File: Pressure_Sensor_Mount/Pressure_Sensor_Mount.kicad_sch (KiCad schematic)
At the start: 2 parts, among them J1 Conn_01x04_Pin

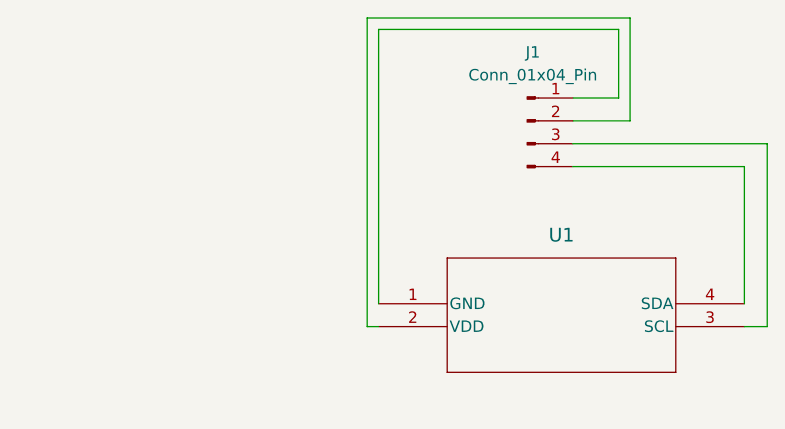
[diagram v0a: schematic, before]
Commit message: Modified boot.py and KiCad Schematic
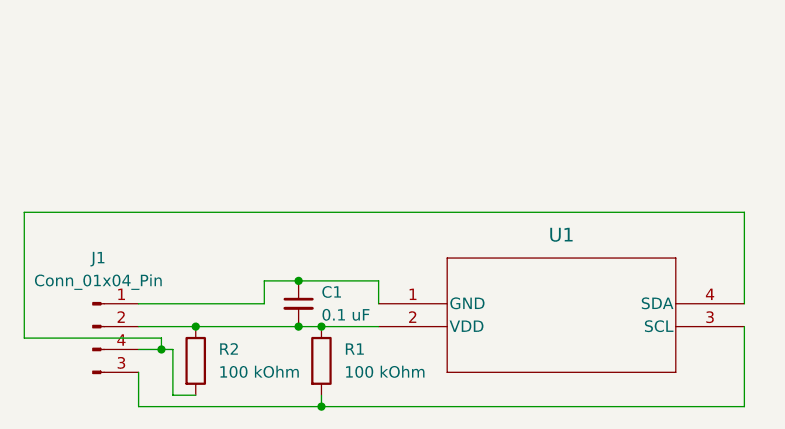
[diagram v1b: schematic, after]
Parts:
- added C1: 0.1 uF, symbol Device:C_Small
- added R1, R2: 100 kOhm, symbol Device:R
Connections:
- net at J1.1 (Pin_1), U1.1 (GND): now also C1.1
- net at J1.2 (Pin_2), U1.2 (VDD): now also C1.2, R1.1, R2.1
- net at J1.3 (Pin_3), U1.3 (SCL): now also R1.2
- net at J1.4 (Pin_4), U1.4 (SDA): now also R2.2
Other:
- moved on the sheet: J1
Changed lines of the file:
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@@
 (kicad_sch (version 20230121) (generator eeschema)
   (paper "A4")
-  (wire (pts (xy 140.97 92.71) (xy 160.02 92.71))
-    (stroke (width 0) (type default))
-  )
-  (wire (pts (xy 162.56 110.49) (xy 160.02 110.49))
-    (stroke (width 0) (type default))
-  )
-  (wire (pts (xy 147.32 76.2) (xy 147.32 87.63))
-    (stroke (width 0) (type default))
-  )
-  (wire (pts (xy 147.32 87.63) (xy 140.97 87.63))
-    (stroke (width 0) (type default))
-  )
-  (wire (pts (xy 160.02 107.95) (xy 160.02 92.71))
-    (stroke (width 0) (type default))
-  )
-  (wire (pts (xy 140.97 90.17) (xy 162.56 90.17))
-    (stroke (width 0) (type default))
-  )
-  (wire (pts (xy 162.56 90.17) (xy 162.56 110.49))
-    (stroke (width 0) (type default))
-  )
-  (wire (pts (xy 119.38 107.95) (xy 119.38 77.47))
-    (stroke (width 0) (type default))
-  )
-  (wire (pts (xy 146.05 77.47) (xy 146.05 85.09))
-    (stroke (width 0) (type default))
-  )
-  (wire (pts (xy 119.38 110.49) (xy 118.11 110.49))
-    (stroke (width 0) (type default))
-  )
-  (wire (pts (xy 118.11 76.2) (xy 147.32 76.2))
-    (stroke (width 0) (type default))
-  )
-  (wire (pts (xy 119.38 77.47) (xy 146.05 77.47))
-    (stroke (width 0) (type default))
-  )
-  (wire (pts (xy 118.11 110.49) (xy 118.11 76.2))
-    (stroke (width 0) (type default))
-  )
-  (wire (pts (xy 146.05 85.09) (xy 140.97 85.09))
+  (junction (at 99.06 110.49) (diameter 0) (color 0 0 0 0)
+  )
+  (junction (at 110.49 105.41) (diameter 0) (color 0 0 0 0)
+  )
+  (junction (at 110.49 110.49) (diameter 0) (color 0 0 0 0)
+  )
+  (junction (at 113.03 119.38) (diameter 0) (color 0 0 0 0)
+  )
+  (junction (at 113.03 110.49) (diameter 0) (color 0 0 0 0)
+  )
+  (junction (at 95.25 113.03) (diameter 0) (color 0 0 0 0)
+  )
+  (wire (pts (xy 110.49 110.49) (xy 113.03 110.49))
+    (stroke (width 0) (type default))
+  )
+  (wire (pts (xy 110.49 105.41) (xy 106.68 105.41))
+    (stroke (width 0) (type default))
+  )
+  (wire (pts (xy 113.03 110.49) (xy 119.38 110.49))
+    (stroke (width 0) (type default))
+  )
+  (wire (pts (xy 80.01 111.76) (xy 80.01 97.79))
+    (stroke (width 0) (type default))
+  )
+  (wire (pts (xy 160.02 110.49) (xy 160.02 119.38))
+    (stroke (width 0) (type default))
+  )
+  (wire (pts (xy 92.71 107.95) (xy 106.68 107.95))
+    (stroke (width 0) (type default))
+  )
+  (wire (pts (xy 95.25 111.76) (xy 80.01 111.76))
+    (stroke (width 0) (type default))
+  )
+  (wire (pts (xy 160.02 119.38) (xy 113.03 119.38))
+    (stroke (width 0) (type default))
+  )
+  (wire (pts (xy 92.71 119.38) (xy 113.03 119.38))
+    (stroke (width 0) (type default))
+  )
+  (wire (pts (xy 113.03 119.38) (xy 113.03 118.11))
+    (stroke (width 0) (type default))
+  )
+  (wire (pts (xy 95.25 113.03) (xy 95.25 111.76))
+    (stroke (width 0) (type default))
+  )
+  (wire (pts (xy 119.38 105.41) (xy 119.38 107.95))
+    (stroke (width 0) (type default))
+  )
+  (wire (pts (xy 160.02 97.79) (xy 160.02 107.95))
+    (stroke (width 0) (type default))
+  )
+  (wire (pts (xy 96.52 118.11) (xy 99.06 118.11))
+    (stroke (width 0) (type default))
+  )
+  (wire (pts (xy 92.71 115.57) (xy 92.71 119.38))
+    (stroke (width 0) (type default))
+  )
+  (wire (pts (xy 95.25 113.03) (xy 96.52 113.03))
+    (stroke (width 0) (type default))
+  )
+  (wire (pts (xy 80.01 97.79) (xy 160.02 97.79))
+    (stroke (width 0) (type default))
+  )
+  (wire (pts (xy 99.06 110.49) (xy 110.49 110.49))
+    (stroke (width 0) (type default))
+  )
+  (wire (pts (xy 110.49 105.41) (xy 119.38 105.41))
+    (stroke (width 0) (type default))
+  )
+  (wire (pts (xy 92.71 113.03) (xy 95.25 113.03))
+    (stroke (width 0) (type default))
+  )
+  (wire (pts (xy 106.68 105.41) (xy 106.68 107.95))
+    (stroke (width 0) (type default))
+  )
+  (wire (pts (xy 96.52 113.03) (xy 96.52 118.11))
+    (stroke (width 0) (type default))
+  )
+  (wire (pts (xy 92.71 110.49) (xy 99.06 110.49))
     (stroke (width 0) (type default))
   )
@@
     (pin "4")
     (instances
-      (project "nanofloat-pressure-sensor-mount"
+      (project "Pressure_Sensor_Mount"
         (path "/36745fa6-eaa2-467e-b9f0-5e9a6d81871a"
           (reference "U1") (unit 1)
@@
     )
   )
-  (symbol (lib_id "Connector:Conn_01x04_Pin") (at 135.89 87.63 0) (unit 1)
+  (symbol (lib_id "Connector:Conn_01x04_Pin") (at 87.63 110.49 0) (unit 1)
     (in_bom yes) (on_board yes) (dnp no) (fields_autoplaced)
-    (property "Reference" "J1" (at 136.525 80.01 0)
+    (property "Reference" "J1" (at 88.265 102.87 0)
       (effects (font (size 1.27 1.27)))
     )
-    (property "Value" "Conn_01x04_Pin" (at 136.525 82.55 0)
+    (property "Value" "Conn_01x04_Pin" (at 88.265 105.41 0)
       (effects (font (size 1.27 1.27)))
     )
-    (property "Footprint" "Connector_PinHeader_2.54mm:PinHeader_1x04_P2.54mm_Vertical" (at 135.89 87.63 0)
-      (effects (font (size 1.27 1.27)) hide)
-    )
-    (property "Datasheet" "~" (at 135.89 87.63 0)
+    (property "Footprint" "Connector_PinHeader_2.54mm:PinHeader_1x04_P2.54mm_Vertical" (at 87.63 110.49 0)
+      (effects (font (size 1.27 1.27)) hide)
+    )
+    (property "Datasheet" "~" (at 87.63 110.49 0)
       (effects (font (size 1.27 1.27)) hide)
     )
@@
     (pin "2")
     (instances
-      (project "nanofloat-pressure-sensor-mount"
+      (project "Pressure_Sensor_Mount"
         (path "/36745fa6-eaa2-467e-b9f0-5e9a6d81871a"
           (reference "J1") (unit 1)
         )
       )
+    )
+  )
+  (symbol (lib_id "Device:C_Small") (at 110.49 107.95 0) (unit 1)
+    (in_bom yes) (on_board yes) (dnp no) (fields_autoplaced)
+    (property "Reference" "C1" (at 113.03 106.6863 0)
+      (effects (font (size 1.27 1.27)) (justify left))
+    )
+    (property "Value" "0.1 uF" (at 113.03 109.2263 0)
+      (effects (font (size 1.27 1.27)) (justify left))
+    )
+    (property "Footprint" "" (at 110.49 107.95 0)
+      (effects (font (size 1.27 1.27)) hide)
+    )
+    (property "Datasheet" "~" (at 110.49 107.95 0)
+      (effects (font (size 1.27 1.27)) hide)
+    )
+    (pin "1")
+    (pin "2")
+    (instances
+      (project "Pressure_Sensor_Mount"
+        (path "/36745fa6-eaa2-467e-b9f0-5e9a6d81871a"
+          (reference "C1") (unit 1)
+        )
+      )
+    )
+  )
+  (symbol (lib_id "Device:R") (at 99.06 114.3 0) (unit 1)
+    (in_bom yes) (on_board yes) (dnp no)
+    (property "Reference" "R2" (at 101.6 113.03 0)
+      (effects (font (size 1.27 1.27)) (justify left))
+    )
+    (property "Value" "100 kOhm" (at 101.6 115.57 0)
+      (effects (font (size 1.27 1.27)) (justify left))
+    )
+    (property "Footprint" "" (at 97.282 114.3 90)
+      (effects (font (size 1.27 1.27)) hide)
+    )
+    (property "Datasheet" "~" (at 99.06 114.3 0)
+      (effects (font (size 1.27 1.27)) hide)
+    )
+    (pin "2")
+    (pin "1")
+    (instances
+      (project "Pressure_Sensor_Mount"
+        (path "/36745fa6-eaa2-467e-b9f0-5e9a6d81871a"
+          (reference "R2") (unit 1)
+        )
+      )
+    )
+  )
+  (symbol (lib_id "Device:R") (at 113.03 114.3 0) (unit 1)
+    (in_bom yes) (on_board yes) (dnp no)
+    (property "Reference" "R1" (at 115.57 113.03 0)
+      (effects (font (size 1.27 1.27)) (justify left))
+    )
+    (property "Value" "100 kOhm" (at 115.57 115.57 0)
+      (effects (font (size 1.27 1.27)) (justify left))
+    )
+    (property "Footprint" "" (at 111.252 114.3 90)
+      (effects (font (size 1.27 1.27)) hide)
+    )
+    (property "Datasheet" "~" (at 113.03 114.3 0)
+      (effects (font (size 1.27 1.27)) hide)
+    )
+    (pin "2")
+    (pin "1")
+    (instances
+      (project "Pressure_Sensor_Mount"
+        (path "/36745fa6-eaa2-467e-b9f0-5e9a6d81871a"
+          (reference "R1") (unit 1)
+        )
+      )
